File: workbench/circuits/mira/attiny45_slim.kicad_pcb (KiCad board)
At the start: 2 copper layers, 16.5 x 19.1 mm, 9 parts, among them IC1 ATTINY45-P, Q1 RLB3034

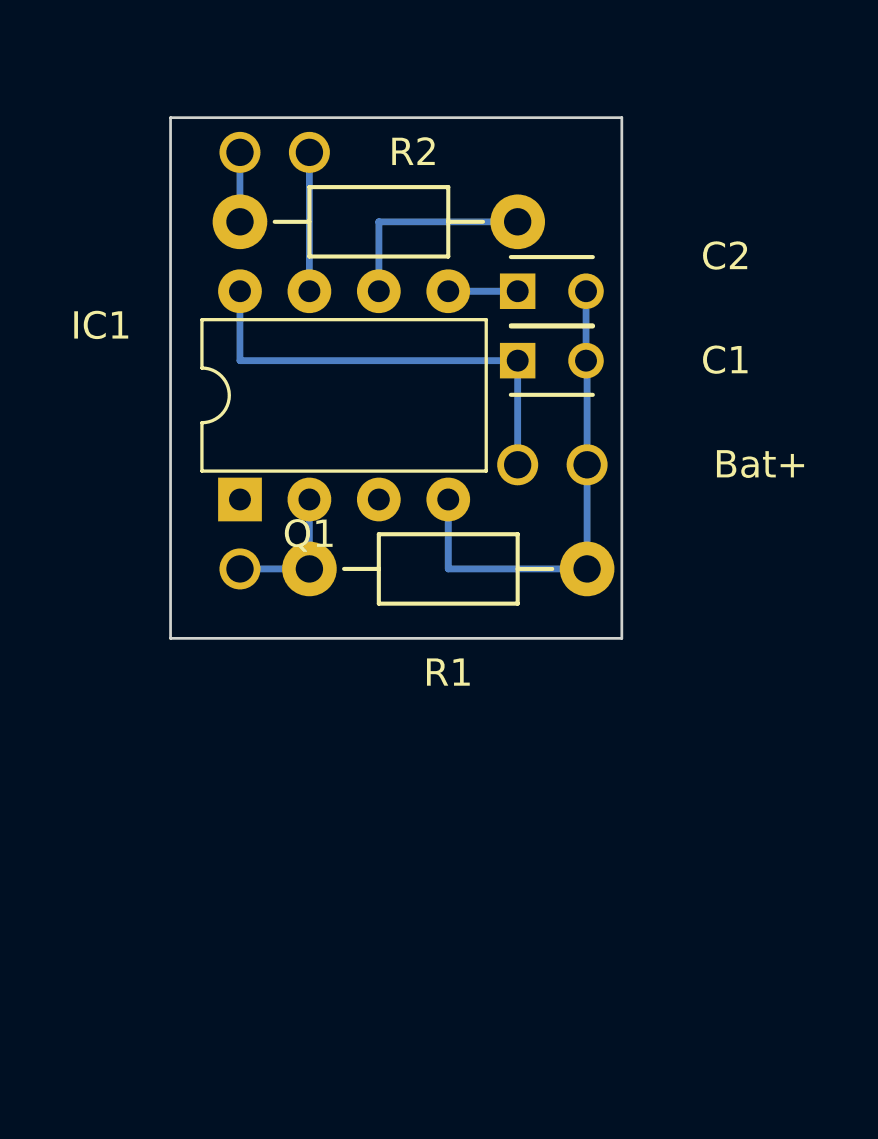
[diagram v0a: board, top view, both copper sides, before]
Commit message: Cleaned up the Mira KiCad files... ... and moved them to an approproate subdirectory. Added the Mira "slim" PCB. Removed an old Sphinx page and moved the Sphinx project logo.
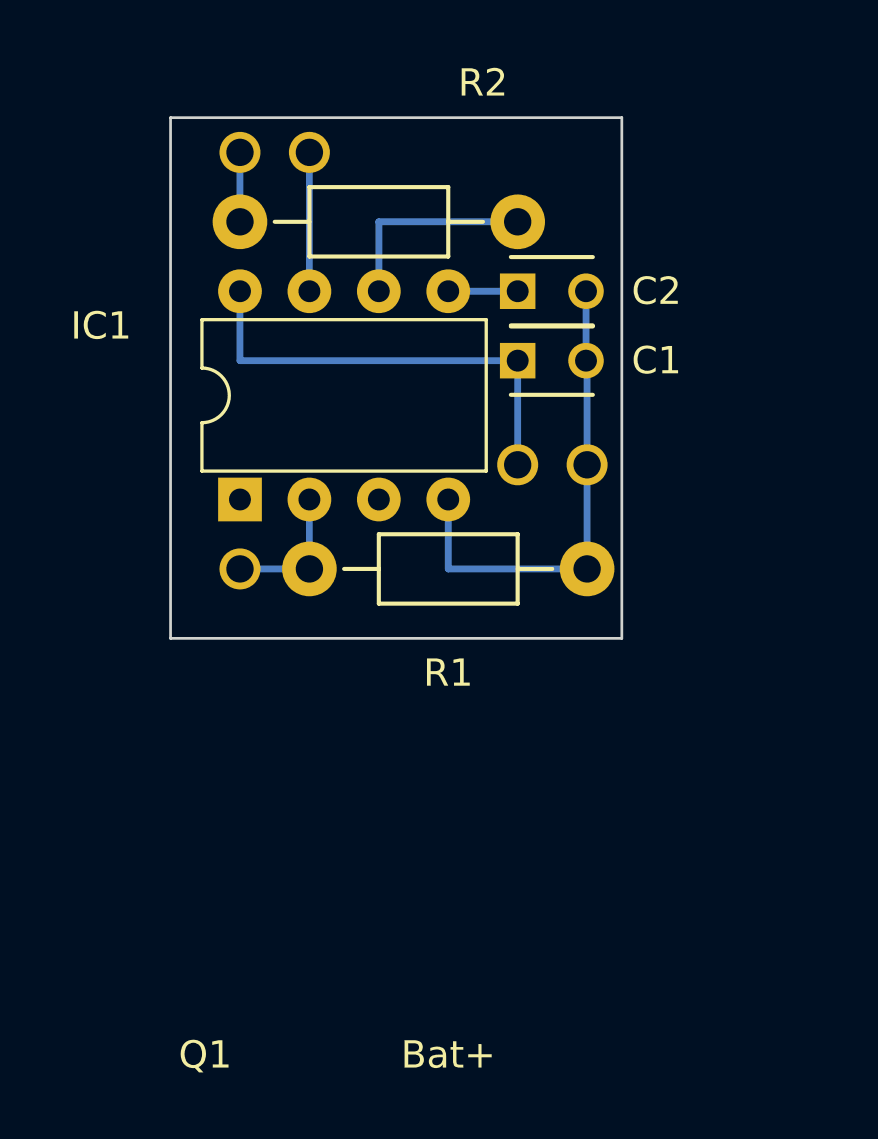
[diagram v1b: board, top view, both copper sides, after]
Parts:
- R1: value 22kΩ -> 15kΩ
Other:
- net class Thick added: clearance 0.2, trace_width 0.5, via_dia 0.6, via_drill 0.4
- board text added: "Batt + / Batt −"
